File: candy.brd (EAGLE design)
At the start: 100 x 80 mm, 8 parts

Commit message: sch
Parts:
- U$2: value N-MOSFET -> N-MOSFETREGULAR; device TinyTony_ShenzenReady:SOT323-CANDY -> TinyTony_ShenzenReady:SOT323
- moved U$7 15.6 mm to (15.1, 23.1)
- moved U$1 14.1 mm to (6.23, 19.0)
- moved U$4 11.7 mm to (15.2, 28.9)
- moved U$3 8.66 mm to (23.0, 19.0), turned to 0 degrees
- moved U$6 5.70 mm to (6.66, 28.6)
- moved U$5 4.92 mm to (23.6, 28.6)
- moved R1 1.50 mm to (15.2, 15.0), turned to 0 degrees
- moved U$2 0.38 mm to (15.2, 19.9)
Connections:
- net GND: now also U$2.2S; no longer U$2.3
- net N$1: now also U$2.1G; no longer U$2.2
- net N$3: now also U$2.3D; no longer U$2.1
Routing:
- net VCC: track 0.00 -> 32.3 mm, vias 0 -> 2
- net GND: track 0.00 -> 20.9 mm, vias 0 -> 1
- net N$1: track 0.00 -> 13.3 mm
- net N$3: track 0.00 -> 8.00 mm
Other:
- board size 100 x 80 mm -> 26 x 26 mm
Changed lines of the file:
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@@
 <setting verticaltext="up"/>
 </settings>
-<grid distance="50" unitdist="mil" unit="mil" style="lines" multiple="1" display="yes" altdistance="5" altunitdist="mil" altunit="mil"/>
+<grid distance="0.500000001" unitdist="mm" unit="mm" style="lines" multiple="1" display="yes" altdistance="5" altunitdist="mil" altunit="mil"/>
 <layers>
 <layer number="1" name="Top" color="4" fill="1" visible="yes" active="yes"/>
@@
 <layer number="27" name="tValues" color="7" fill="1" visible="yes" active="yes"/>
 <layer number="28" name="bValues" color="7" fill="1" visible="yes" active="yes"/>
-<layer number="29" name="tStop" color="7" fill="3" visible="no" active="yes"/>
-<layer number="30" name="bStop" color="7" fill="6" visible="no" active="yes"/>
-<layer number="31" name="tCream" color="7" fill="4" visible="no" active="yes"/>
+<layer number="29" name="tStop" color="7" fill="3" visible="yes" active="yes"/>
+<layer number="30" name="bStop" color="7" fill="6" visible="yes" active="yes"/>
+<layer number="31" name="tCream" color="7" fill="4" visible="yes" active="yes"/>
 <layer number="32" name="bCream" color="7" fill="5" visible="no" active="yes"/>
 <layer number="33" name="tFinish" color="6" fill="3" visible="no" active="yes"/>
@@
 <layer number="44" name="Drills" color="7" fill="1" visible="no" active="yes"/>
 <layer number="45" name="Holes" color="7" fill="1" visible="no" active="yes"/>
-<layer number="46" name="Milling" color="3" fill="1" visible="no" active="yes"/>
-<layer number="47" name="Measures" color="7" fill="1" visible="no" active="yes"/>
+<layer number="46" name="Milling" color="3" fill="1" visible="yes" active="yes"/>
+<layer number="47" name="Measures" color="7" fill="1" visible="yes" active="yes"/>
 <layer number="48" name="Document" color="7" fill="1" visible="yes" active="yes"/>
 <layer number="49" name="Reference" color="7" fill="1" visible="yes" active="yes"/>
@@
 <board>
 <plain>
-<wire x1="0" y1="0" x2="100" y2="0" width="0" layer="20"/>
-<wire x1="100" y1="0" x2="100" y2="80" width="0" layer="20"/>
-<wire x1="100" y1="80" x2="0" y2="80" width="0" layer="20"/>
-<wire x1="0" y1="80" x2="0" y2="0" width="0" layer="20"/>
+<rectangle x1="13.7287" y1="20.4978" x2="16.7287" y2="22.9978" layer="1"/>
+<rectangle x1="4.75" y1="26.75" x2="9.25" y2="30.75" layer="1" rot="R90"/>
+<rectangle x1="13.024040625" y1="26.752359375" x2="17.524040625" y2="30.752359375" layer="1" rot="R90"/>
+<rectangle x1="21.024040625" y1="26.752359375" x2="25.524040625" y2="30.752359375" layer="1" rot="R90"/>
+<rectangle x1="20.997640625" y1="16.774040625" x2="25.497640625" y2="20.774040625" layer="1" rot="R180"/>
+<rectangle x1="4.002359375" y1="17.225959375" x2="8.502359375" y2="21.225959375" layer="1"/>
+<circle x="15" y="23" radius="13" width="0.2032" layer="20"/>
+<rectangle x1="12" y1="18" x2="15" y2="19.5" layer="1"/>
+<rectangle x1="15.5" y1="18" x2="18.5" y2="19.5" layer="1"/>
+<rectangle x1="5" y1="26.5" x2="9" y2="31" layer="29"/>
+<rectangle x1="13.081" y1="26.416" x2="17.399" y2="31.115" layer="29"/>
+<rectangle x1="21.082" y1="26.416" x2="25.4" y2="31.242" layer="29"/>
+<rectangle x1="3.937" y1="17.145" x2="8.636" y2="21.336" layer="29"/>
+<rectangle x1="20.955" y1="16.637" x2="25.654" y2="20.828" layer="29"/>
+<rectangle x1="13.716" y1="20.447" x2="16.764" y2="23.114" layer="29"/>
+<rectangle x1="11.938" y1="17.907" x2="15.113" y2="19.558" layer="29"/>
+<rectangle x1="15.494" y1="17.907" x2="18.542" y2="19.558" layer="29"/>
+<rectangle x1="5" y1="26.5" x2="9" y2="31" layer="31"/>
+<rectangle x1="13.081" y1="26.416" x2="17.399" y2="31.115" layer="31"/>
+<rectangle x1="21.082" y1="26.416" x2="25.4" y2="31.242" layer="31"/>
+<rectangle x1="20.955" y1="16.637" x2="25.654" y2="20.828" layer="31"/>
+<rectangle x1="3.937" y1="17.145" x2="8.636" y2="21.336" layer="31"/>
+<rectangle x1="11.938" y1="17.907" x2="15.113" y2="19.558" layer="31"/>
+<rectangle x1="15.494" y1="17.907" x2="18.542" y2="19.558" layer="31"/>
+<rectangle x1="13.716" y1="20.447" x2="16.764" y2="23.114" layer="31"/>
 </plain>
 <attributes>
@@
 </autorouter>
 <elements>
-<element name="U$1" library="TinyTony_ShenzenReady" package="PADSMD" value="SMDPAD" x="20.32" y="19.05"/>
-<element name="U$2" library="TinyTony_ShenzenReady" package="SOT323-CANDY" value="N-MOSFET" x="15.24" y="20.32" smashed="yes"/>
-<element name="U$3" library="TinyTony_ShenzenReady" package="PADSMD" value="SMDPAD" x="15.24" y="22.86" rot="R90"/>
-<element name="U$4" library="TinyTony_ShenzenReady" package="PADSMD" value="SMDPAD" x="8.89" y="19.05"/>
-<element name="R1" library="adafruit" library_urn="urn:adsk.eagle:library:420" package="R1206" value="" x="15.24" y="16.51" smashed="yes" rot="R180">
-<attribute name="VALUE" x="16.637" y="18.923" size="1.27" layer="27" rot="R180"/>
+<element name="U$1" library="TinyTony_ShenzenReady" package="PADSMD" value="SMDPAD" x="6.2279375" y="19.019521875"/>
+<element name="U$2" library="TinyTony_ShenzenReady" package="SOT323" value="N-MOSFETREGULAR" x="15.24" y="19.939" smashed="yes"/>
+<element name="U$3" library="TinyTony_ShenzenReady" package="PADSMD" value="SMDPAD" x="23.000978125" y="19.006821875"/>
+<element name="U$4" library="TinyTony_ShenzenReady" package="PADSMD" value="SMDPAD" x="15.24" y="28.86"/>
+<element name="R1" library="adafruit" library_urn="urn:adsk.eagle:library:420" package="R1206" value="" x="15.24" y="15.01" smashed="yes">
+<attribute name="VALUE" x="13.843" y="12.597" size="1.27" layer="27"/>
 </element>
-<element name="U$5" library="TinyTony_ShenzenReady" package="PADSMD" value="SMDPAD" x="21.59" y="24.13"/>
-<element name="U$6" library="TinyTony_ShenzenReady" package="PADSMD" value="SMDPAD" x="10.16" y="24.13"/>
-<element name="U$7" library="TinyTony_ShenzenReady" package="LINX" value="" x="16.637" y="7.62" rot="MR0"/>
+<element name="U$5" library="TinyTony_ShenzenReady" package="PADSMD" value="SMDPAD" x="23.59" y="28.63"/>
+<element name="U$6" library="TinyTony_ShenzenReady" package="PADSMD" value="SMDPAD" x="6.66" y="28.63"/>
+<element name="U$7" library="TinyTony_ShenzenReady" package="LINX" value="" x="15.137" y="23.12" rot="MR0"/>
 </elements>
 <signals>
 <signal name="N$1">
-<contactref element="U$2" pad="2"/>
+<contactref element="U$2" pad="1G"/>
 <contactref element="U$1" pad="P$1"/>
 <contactref element="R1" pad="1"/>
-<wire x1="15.89" y1="19.395" x2="16.662" y2="16.51" width="0" layer="19" extent="1-1"/>
-<wire x1="20.32" y1="19.05" x2="15.89" y2="19.395" width="0" layer="19" extent="1-1"/>
+<wire x1="6.2279375" y1="19.019521875" x2="14.584478125" y2="19.019521875" width="0.4064" layer="1"/>
+<wire x1="14.584478125" y1="19.019521875" x2="14.59" y2="19.014" width="0.2032" layer="1"/>
+<wire x1="14.59" y1="19.014" x2="13.716" y2="19.05" width="0.4064" layer="1"/>
+<wire x1="13.716" y1="19.05" x2="13.818" y2="15.01" width="0.4064" layer="1"/>
 </signal>
 <signal name="N$3">
-<contactref element="U$2" pad="1"/>
+<contactref element="U$2" pad="3D"/>
 <contactref element="U$4" pad="P$1"/>
-<wire x1="8.89" y1="19.05" x2="14.59" y2="19.395" width="0" layer="19" extent="1-1"/>
+<wire x1="15.24" y1="20.864" x2="15.24" y2="28.86" width="0.4064" layer="1"/>
 </signal>
 <signal name="GND">
 <contactref element="U$7" pad="P$1-"/>
-<contactref element="U$2" pad="3"/>
+<contactref element="U$2" pad="2S"/>
 <contactref element="U$3" pad="P$1"/>
 <contactref element="R1" pad="2"/>
-<wire x1="13.818" y1="16.51" x2="16.637" y2="7.62" width="0" layer="19" extent="1-1"/>
-<wire x1="15.24" y1="21.245" x2="13.818" y2="16.51" width="0" layer="19" extent="1-1"/>
-<wire x1="15.24" y1="22.86" x2="15.24" y2="21.245" width="0" layer="19" extent="1-1"/>
+<wire x1="22.000009375" y1="19.00783125" x2="23.000978125" y2="19.006821875" width="0.4064" layer="1"/>
+<wire x1="15.89" y1="19.014" x2="16.637" y2="19.05" width="0.4064" layer="1"/>
+<wire x1="16.637" y1="19.05" x2="16.662" y2="15.01" width="0.4064" layer="1"/>
+<wire x1="15.89" y1="19.014" x2="22.000009375" y2="19.00783125" width="0.4064" layer="1"/>
+<wire x1="23.000978125" y1="19.006821875" x2="21.971" y2="19.939" width="0.4064" layer="1"/>
+<wire x1="21.971" y1="19.939" x2="22" y2="20" width="0.2032" layer="1"/>
+<via x="22" y="20" extent="1-16" drill="0.35"/>
+<wire x1="22" y1="20" x2="15.137" y2="23.12" width="0.2032" layer="16"/>
 </signal>
 <signal name="VCC">
@@
 <contactref element="U$7" pad="P$3+"/>
 <contactref element="U$7" pad="P$2+"/>
-<wire x1="27.94" y1="7.62" x2="5.334" y2="7.62" width="0" layer="19" extent="1-1"/>
-<wire x1="21.59" y1="24.13" x2="27.94" y2="7.62" width="0" layer="19" extent="1-1"/>
-<wire x1="10.16" y1="24.13" x2="21.59" y2="24.13" width="0" layer="19" extent="1-1"/>
+<wire x1="23.59" y1="28.63" x2="26.5" y2="23.627" width="0.4064" layer="1"/>
+<via x="26.5" y="23.627" extent="1-16" drill="0.35"/>
+<wire x1="26.5" y1="23.627" x2="26.44" y2="23.12" width="0.4064" layer="16"/>
+<wire x1="3.834" y1="23.12" x2="3.992" y2="23.627" width="0.4064" layer="16"/>
+<via x="3.992" y="23.627" extent="1-16" drill="0.35"/>
+<wire x1="5.238" y1="25.746" x2="3.992" y2="23.627" width="0.4064" layer="1"/>
+<wire x1="6.66" y1="28.63" x2="5.238" y2="25.746" width="0.4064" layer="1"/>
+<wire x1="6.66" y1="28.63" x2="10" y2="32" width="0.4064" layer="1"/>
+<wire x1="10" y1="32" x2="20.5" y2="32" width="0.4064" layer="1"/>
+<wire x1="20.5" y1="32" x2="23.59" y2="28.63" width="0.4064" layer="1"/>
 </signal>
 </signals>
@@
 with this version.
 </note>
+<note version="8.3" severity="warning">
+Since Version 8.3, EAGLE supports URNs for individual library
+assets (packages, symbols, and devices). The URNs of those assets
+will not be understood (or retained) with this version.
+</note>
 </compatibility>

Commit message: with ugly polygons on layout
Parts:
- U$7: device TinyTony_ShenzenReady:LINX -> TinyTony_ShenzenReady:CR2032-LINX
- moved U$7 0.71 mm to (14.6, 22.6)
- moved U$2 0.50 mm to (15.2, 20.4)
- renumbered U$6 to VCC
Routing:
- net GND: track 20.9 -> 0.00 mm, vias 1 -> 0
- net VCC: track 32.3 -> 20.5 mm, vias 2 -> 4
- net N$3: track 8.00 -> 7.50 mm
- added copper zone on layer 16, net GND
- added copper zone on layer 1, net VCC
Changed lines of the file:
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@@
 <?xml version="1.0" encoding="utf-8"?>
 <!DOCTYPE eagle SYSTEM "eagle.dtd">
-<eagle version="8.6.0">
+<eagle version="8.7.0">
 <drawing>
 <settings>
@@
 <setting verticaltext="up"/>
 </settings>
-<grid distance="0.500000001" unitdist="mm" unit="mm" style="lines" multiple="1" display="yes" altdistance="5" altunitdist="mil" altunit="mil"/>
+<grid distance="19.6850394" unitdist="mil" unit="mil" style="lines" multiple="1" display="yes" altdistance="5" altunitdist="mil" altunit="mil"/>
 <layers>
 <layer number="1" name="Top" color="4" fill="1" visible="yes" active="yes"/>
@@
 <elements>
 <element name="U$1" library="TinyTony_ShenzenReady" package="PADSMD" value="SMDPAD" x="6.2279375" y="19.019521875"/>
-<element name="U$2" library="TinyTony_ShenzenReady" package="SOT323" value="N-MOSFETREGULAR" x="15.24" y="19.939" smashed="yes"/>
+<element name="U$2" library="TinyTony_ShenzenReady" package="SOT323" value="N-MOSFETREGULAR" x="15.24" y="20.439" smashed="yes"/>
 <element name="U$3" library="TinyTony_ShenzenReady" package="PADSMD" value="SMDPAD" x="23.000978125" y="19.006821875"/>
 <element name="U$4" library="TinyTony_ShenzenReady" package="PADSMD" value="SMDPAD" x="15.24" y="28.86"/>
@@
 </element>
 <element name="U$5" library="TinyTony_ShenzenReady" package="PADSMD" value="SMDPAD" x="23.59" y="28.63"/>
-<element name="U$6" library="TinyTony_ShenzenReady" package="PADSMD" value="SMDPAD" x="6.66" y="28.63"/>
-<element name="U$7" library="TinyTony_ShenzenReady" package="LINX" value="" x="15.137" y="23.12" rot="MR0"/>
+<element name="VCC" library="TinyTony_ShenzenReady" package="PADSMD" value="SMDPAD" x="6.66" y="28.63"/>
+<element name="U$7" library="TinyTony_ShenzenReady" library_urn="urn:adsk.eagle:library:2159173" package="CR2032-LINX" package3d_urn="urn:adsk.eagle:package:2160680/2" value="" x="14.637" y="22.62" rot="MR0"/>
 </elements>
 <signals>
@@
 <contactref element="U$1" pad="P$1"/>
 <contactref element="R1" pad="1"/>
-<wire x1="6.2279375" y1="19.019521875" x2="14.584478125" y2="19.019521875" width="0.4064" layer="1"/>
-<wire x1="14.584478125" y1="19.019521875" x2="14.59" y2="19.014" width="0.2032" layer="1"/>
-<wire x1="14.59" y1="19.014" x2="13.716" y2="19.05" width="0.4064" layer="1"/>
-<wire x1="13.716" y1="19.05" x2="13.818" y2="15.01" width="0.4064" layer="1"/>
+<wire x1="6.2279375" y1="19.019521875" x2="6.233459375" y2="19.014" width="0.1524" layer="1"/>
+<wire x1="6.233459375" y1="19.014" x2="14.59" y2="19.514" width="0.1524" layer="1"/>
+<wire x1="14.59" y1="19.514" x2="13.818" y2="18.242" width="0.1524" layer="1"/>
+<wire x1="13.818" y1="18.242" x2="13.818" y2="15.01" width="0.1524" layer="1"/>
 </signal>
 <signal name="N$3">
 <contactref element="U$2" pad="3D"/>
 <contactref element="U$4" pad="P$1"/>
-<wire x1="15.24" y1="20.864" x2="15.24" y2="28.86" width="0.4064" layer="1"/>
+<wire x1="15.24" y1="21.364" x2="15.24" y2="28.86" width="0.1524" layer="1"/>
 </signal>
 <signal name="GND">
@@
 <contactref element="U$3" pad="P$1"/>
 <contactref element="R1" pad="2"/>
-<wire x1="22.000009375" y1="19.00783125" x2="23.000978125" y2="19.006821875" width="0.4064" layer="1"/>
-<wire x1="15.89" y1="19.014" x2="16.637" y2="19.05" width="0.4064" layer="1"/>
-<wire x1="16.637" y1="19.05" x2="16.662" y2="15.01" width="0.4064" layer="1"/>
-<wire x1="15.89" y1="19.014" x2="22.000009375" y2="19.00783125" width="0.4064" layer="1"/>
-<wire x1="23.000978125" y1="19.006821875" x2="21.971" y2="19.939" width="0.4064" layer="1"/>
-<wire x1="21.971" y1="19.939" x2="22" y2="20" width="0.2032" layer="1"/>
-<via x="22" y="20" extent="1-16" drill="0.35"/>
-<wire x1="22" y1="20" x2="15.137" y2="23.12" width="0.2032" layer="16"/>
+<polygon width="0.1524" layer="16">
+<vertex x="1" y="37"/>
+<vertex x="1" y="9"/>
+<vertex x="2" y="9"/>
+<vertex x="30" y="9"/>
+<vertex x="30" y="37.5"/>
+<vertex x="1.5" y="37.5"/>
+<vertex x="1.5" y="36.5"/>
+</polygon>
+<wire x1="15.89" y1="19.514" x2="23.000978125" y2="19.006821875" width="0" layer="19" extent="1-1"/>
+<wire x1="14.637" y1="22.62" x2="15.89" y2="19.514" width="0" layer="19" extent="1-16"/>
+<wire x1="16.662" y1="15.01" x2="15.89" y2="19.514" width="0" layer="19" extent="1-1"/>
 </signal>
 <signal name="VCC">
 <contactref element="U$5" pad="P$1"/>
-<contactref element="U$6" pad="P$1"/>
+<contactref element="VCC" pad="P$1"/>
+<polygon width="0.1524" layer="1" isolate="0.3048">
+<vertex x="2" y="29.5"/>
+<vertex x="2" y="9.5"/>
+<vertex x="29" y="9.5"/>
+<vertex x="29" y="36.5"/>
+<vertex x="2.5" y="36.5"/>
+<vertex x="2" y="36.5"/>
+</polygon>
 <contactref element="U$7" pad="P$3+"/>
 <contactref element="U$7" pad="P$2+"/>
-<wire x1="23.59" y1="28.63" x2="26.5" y2="23.627" width="0.4064" layer="1"/>
-<via x="26.5" y="23.627" extent="1-16" drill="0.35"/>
-<wire x1="26.5" y1="23.627" x2="26.44" y2="23.12" width="0.4064" layer="16"/>
-<wire x1="3.834" y1="23.12" x2="3.992" y2="23.627" width="0.4064" layer="16"/>
-<via x="3.992" y="23.627" extent="1-16" drill="0.35"/>
-<wire x1="5.238" y1="25.746" x2="3.992" y2="23.627" width="0.4064" layer="1"/>
-<wire x1="6.66" y1="28.63" x2="5.238" y2="25.746" width="0.4064" layer="1"/>
-<wire x1="6.66" y1="28.63" x2="10" y2="32" width="0.4064" layer="1"/>
-<wire x1="10" y1="32" x2="20.5" y2="32" width="0.4064" layer="1"/>
-<wire x1="20.5" y1="32" x2="23.59" y2="28.63" width="0.4064" layer="1"/>
+<wire x1="3.334" y1="22.62" x2="5.12" y2="22.62" width="0.1524" layer="16"/>
+<wire x1="5.12" y1="22.62" x2="5.5" y2="23" width="0.1524" layer="16"/>
+<via x="5.5" y="23" extent="1-16" drill="0.35"/>
+<wire x1="5.5" y1="23" x2="5.5" y2="27.47" width="0.1524" layer="1"/>
+<wire x1="5.5" y1="27.47" x2="6.66" y2="28.63" width="0.1524" layer="1"/>
+<wire x1="23.59" y1="28.63" x2="22.46" y2="27.5" width="0.1524" layer="1" curve="-90"/>
+<wire x1="22.46" y1="27.5" x2="22" y2="27.5" width="0.1524" layer="1"/>
+<via x="22" y="27.5" extent="1-16" drill="0.35"/>
+<wire x1="6.66" y1="28.63" x2="6.79" y2="28.5" width="0.1524" layer="1" curve="90"/>
+<via x="8.5" y="28.5" extent="1-16" drill="0.35"/>
+<wire x1="6.79" y1="28.5" x2="8.5" y2="28.5" width="0.1524" layer="1"/>
+<wire x1="25.94" y1="22.62" x2="25.82" y2="22.5" width="0.1524" layer="16" curve="-90"/>
+<wire x1="25.82" y1="22.5" x2="23.5" y2="22.5" width="0.1524" layer="16"/>
+<via x="23.5" y="22.5" extent="1-16" drill="0.35"/>
+<wire x1="23.5" y1="22.5" x2="22" y2="24" width="0.1524" layer="1" curve="-90"/>
+<wire x1="22" y1="24" x2="22" y2="27.5" width="0.1524" layer="1"/>
 </signal>
 </signals>
@@
 will not be understood (or retained) with this version.
 </note>
+<note version="8.3" severity="warning">
+Since Version 8.3, EAGLE supports the association of 3D packages
+with devices in libraries, schematics, and board files. Those 3D
+packages will not be understood (or retained) with this version.
+</note>
 </compatibility>

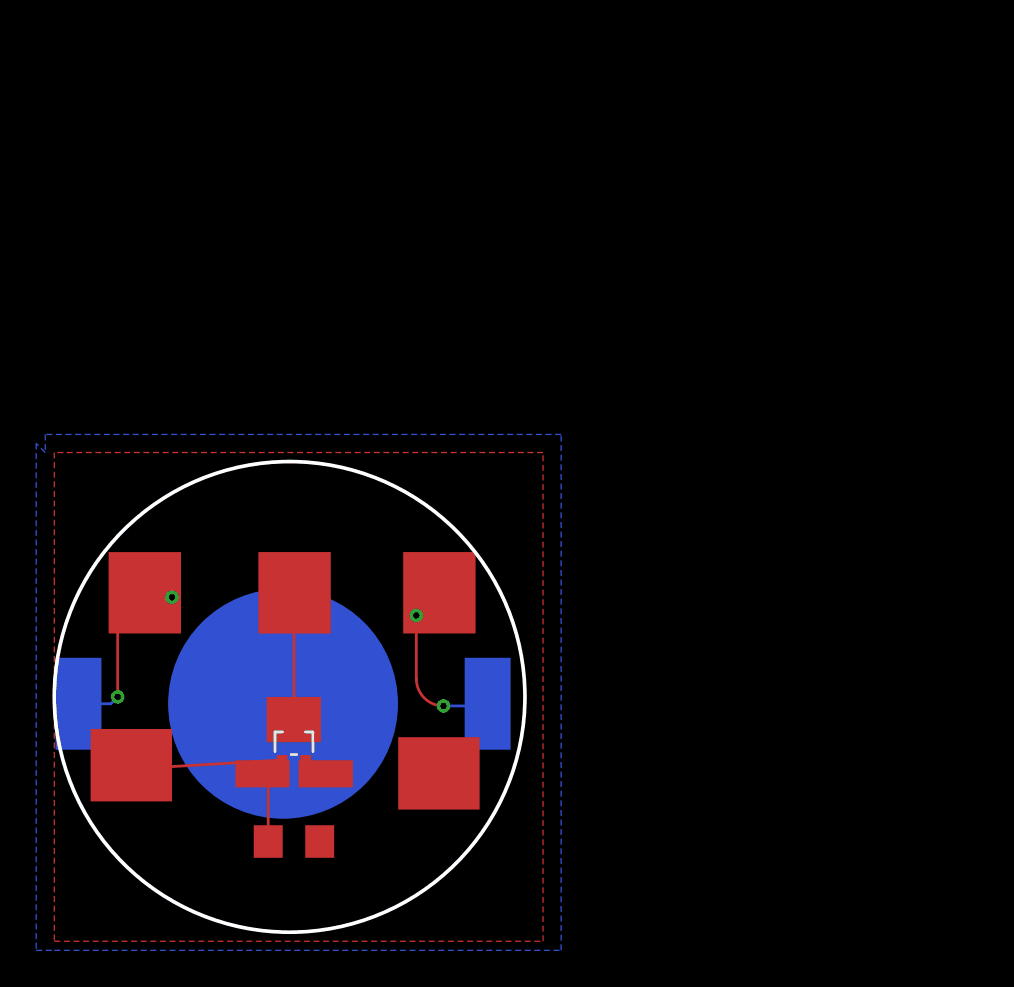
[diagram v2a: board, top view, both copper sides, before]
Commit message: fixed schema and added 2n222
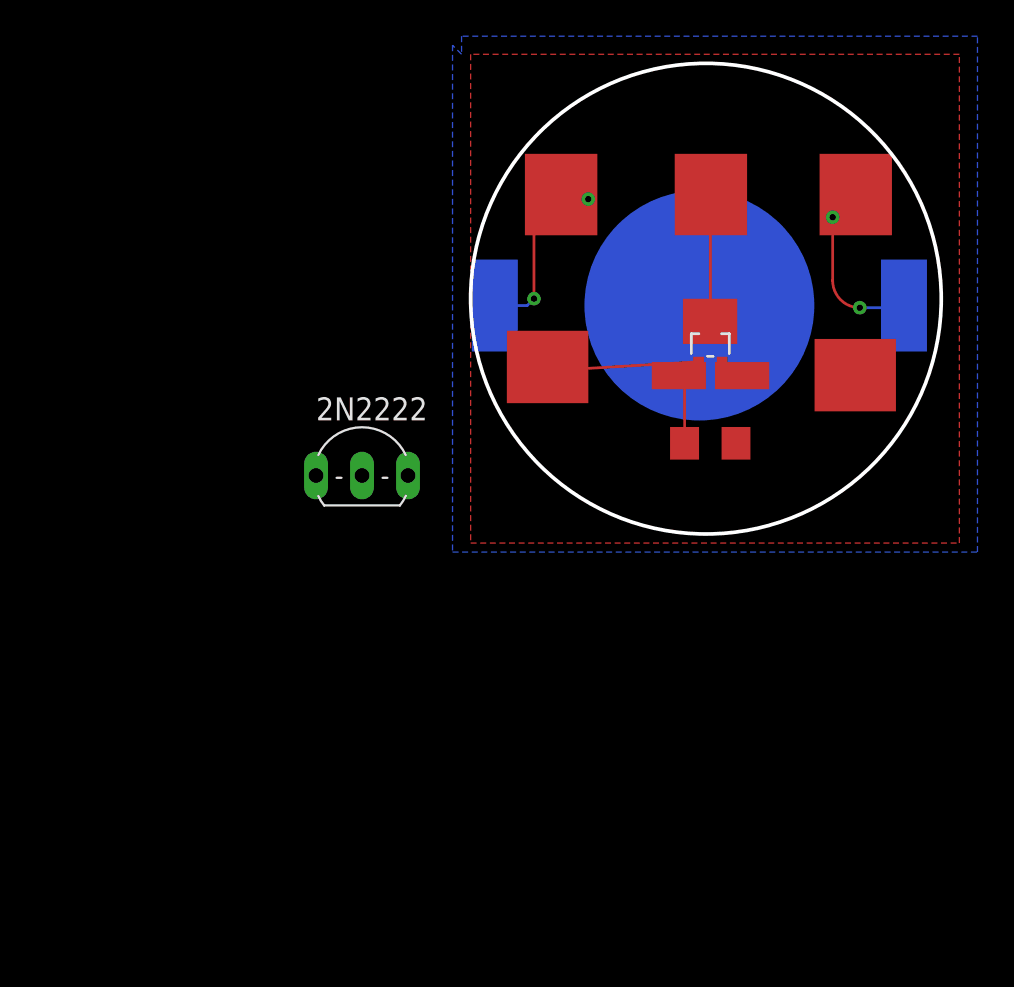
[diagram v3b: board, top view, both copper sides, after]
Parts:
- removed R1: (no value), adafruit:R1206
- removed U$2: N-MOSFETREGULAR, TinyTony_ShenzenReady:SOT323
- removed U$3: SMDPAD, TinyTony_ShenzenReady:PADSMD
- added 10M: (no value), adafruit:R1206
- added 2N2222: (no value), transistor-neu-to92:TO92-EBC
- added N-MOSFET: n-mosfet, TinyTony_ShenzenReady:SOT323
- moved U$1 31.8 mm to (29.2, 41.0)
- moved U$5 31.8 mm to (46.6, 50.6)
- moved VCC 31.8 mm to (29.7, 50.6)
- moved U$4 31.8 mm to (38.2, 50.9)
- moved U$7 31.8 mm to (37.6, 44.6)
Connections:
- removed net N$3: U$2.3D, U$4.P$1
- new net LOAD: 2N2222.E, N-MOSFET.3D, U$4.P$1
- net GND: now also 10M.2, 2N2222.C, N-MOSFET.2S; no longer R1.2, U$2.2S, U$3.P$1
- net N$1: now also 10M.1, 2N2222.B, N-MOSFET.1G; no longer R1.1, U$2.1G
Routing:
- net LOAD: track 0.00 -> 7.50 mm
- net N$3: track 7.50 -> 0.00 mm
